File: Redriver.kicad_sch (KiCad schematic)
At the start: 126 parts, among them U1 DS320PR810NJXR, U2 DS320PR810NJXR

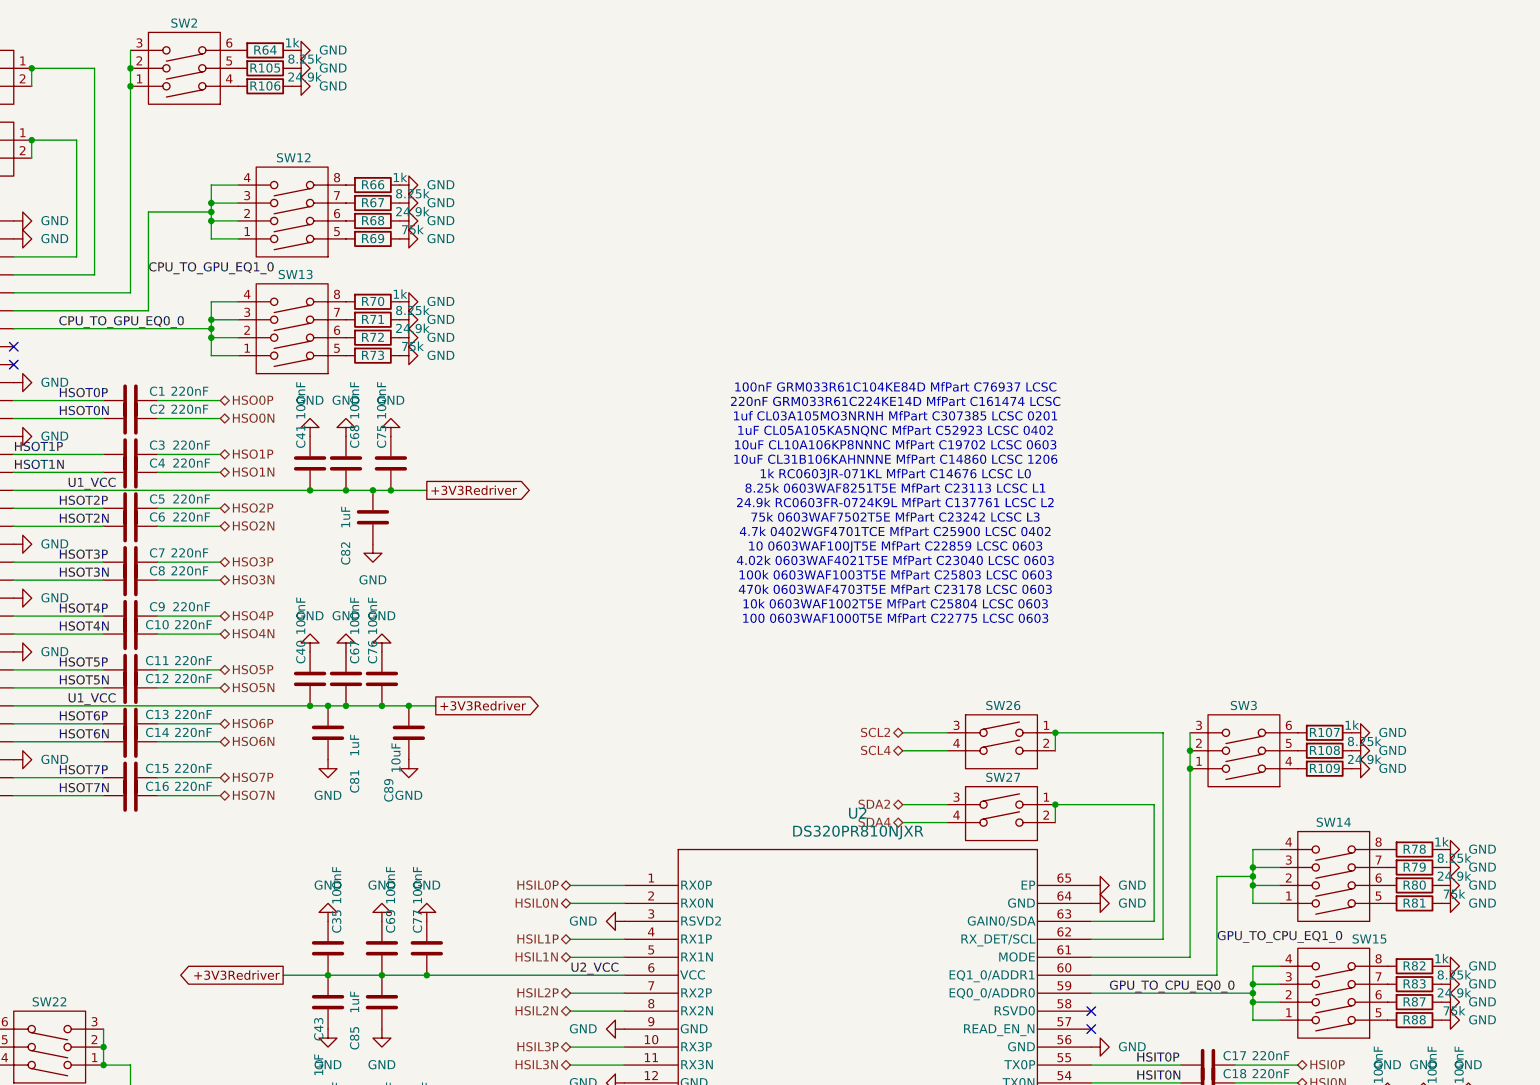
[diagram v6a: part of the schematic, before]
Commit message: removed uneeded mode
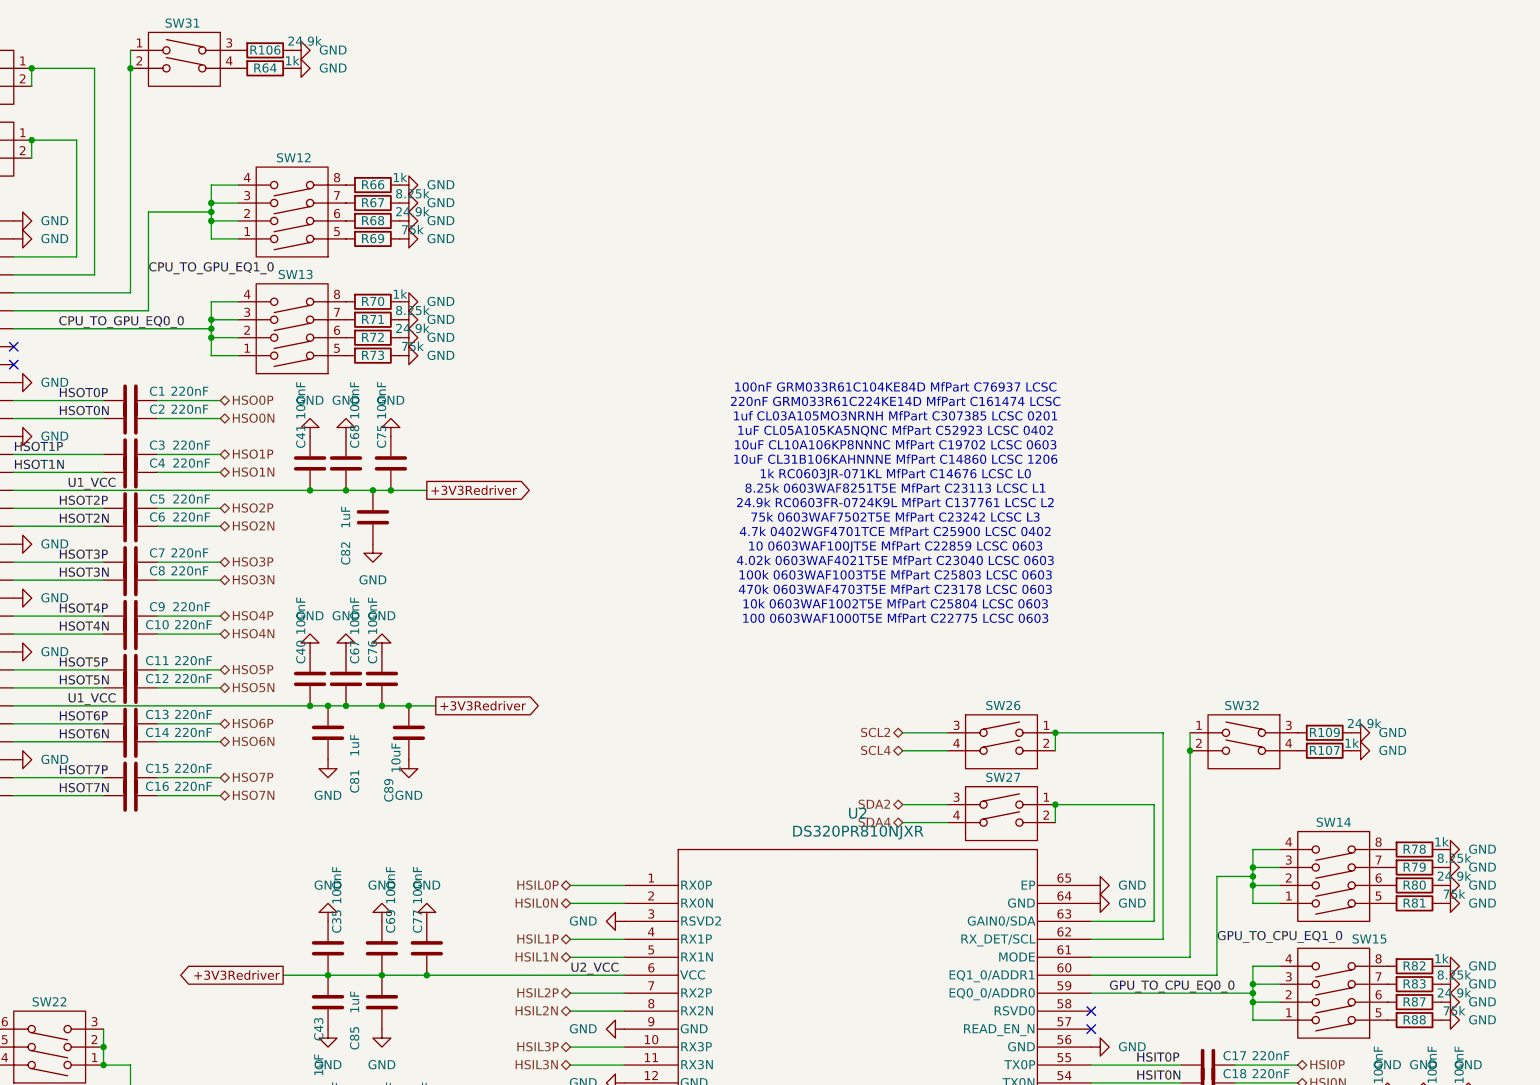
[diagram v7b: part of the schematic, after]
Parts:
- removed R105, R108: 8.25k, Resistor_SMD:R_0603_1608Metric, symbol Device:R
- removed SW2, SW3: ~, DSWB03LHGET:SW-TH_DSWB03LHGET, symbol DSWB03LHGET:DSWB03LHGET
- added SW31, SW32: ~, DSWB02LHGET:SW-TH_DSWB02LHGET, symbol DSWB02LHGET:DSWB02LHGET
- R106, R109: Part_Number 0603WAF8251T5E -> RC0603FR-0724K9L
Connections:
- net at R106.2: now also SW31.3
- net at U1.61 (MODE): now also SW31.1, SW31.2
- net at R64.2: now also SW31.4
- net at R107.2: now also SW32.4
- net at U2.61 (MODE): now also SW32.1, SW32.2
- net at R109.2: now also SW32.3
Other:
- moved on the sheet: R106, R107, R109, R64

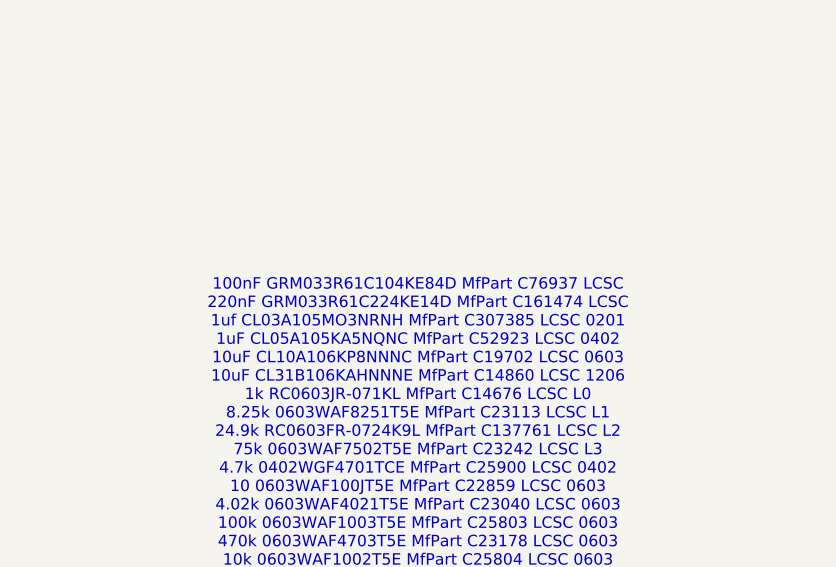
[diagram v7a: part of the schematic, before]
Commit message: added  better components
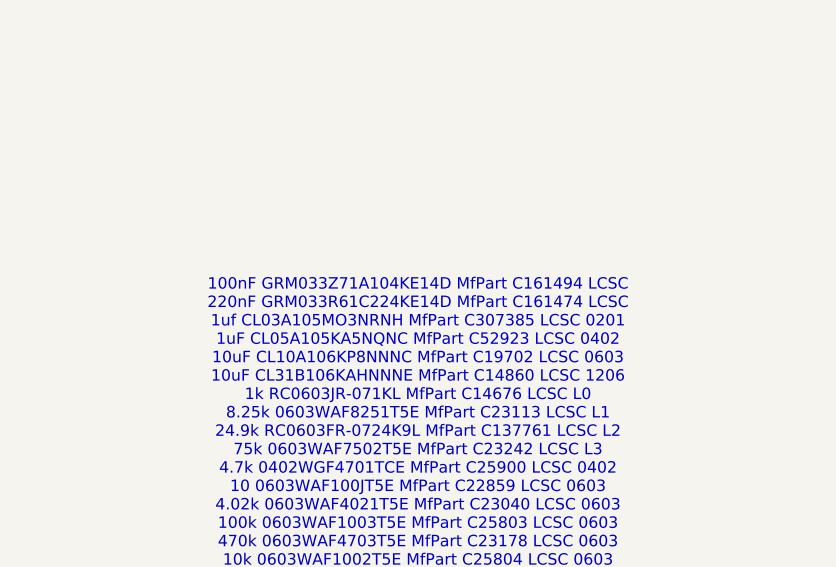
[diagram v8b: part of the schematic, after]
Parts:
- C33, C34, C35, C36, C38, C39, C40, C41, C65, C66, C67, C68, C69, C70, C71, C72, C73, C74, C75, C76, C77, C78, C79, C80: LCSC C76937 -> C161494; Part_Number GRM033R61C104KE84D -> GRM033Z71A104KE14D
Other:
- note added: "100nF GRM033Z71A104KE14D MfPart C161494 LCSC 220nF GRM033R61C224KE14D MfPart C161474 LCSC 1uf CL03A105MO3NRNH MfPart C307385 LCSC 0201 1uF CL05A105KA5NQNC MfPart C52923 LCSC 0402 10uF CL10A106KP8NNNC MfPart C19702 LCSC 0603 10uF CL31B106KAHNNNE MfPart C14860 LCSC 1206 1k RC0603JR-071KL MfPart C14676 LCSC L0 8.25k 0603WAF8251T5E MfPart C23113 LCSC L1 24.9k RC0603FR-0724K9L MfPart C137761 LCSC L2 7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"
- note removed: "100nF GRM033R61C104KE84D MfPart C76937 LCSC 220nF GRM033R61C224KE14D MfPart C161474 LCSC 1uf CL03A105MO3NRNH MfPart C307385 LCSC 0201 1uF CL05A105KA5NQNC MfPart C52923 LCSC 0402 10uF CL10A106KP8NNNC MfPart C19702 LCSC 0603 10uF CL31B106KAHNNNE MfPart C14860 LCSC 1206 1k RC0603JR-071KL MfPart C14676 LCSC L0 8.25k 0603WAF8251T5E MfPart C23113 LCSC L1 24.9k RC0603FR-0724K9L MfPart C137761 LCSC L2 75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"
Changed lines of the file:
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@@
 	(generator_version "9.0")
 	(paper "A4")
-	(text "100nF GRM033R61C104KE84D MfPart C76937 LCSC\n220nF GRM033R61C224KE14D MfPart C161474 LCSC\n1uf CL03A105MO3NRNH MfPart C307385 LCSC 0201\n1uF CL05A105KA5NQNC MfPart C52923 LCSC 0402\n10uF CL10A106KP8NNNC MfPart C19702 LCSC 0603\n10uF CL31B106KAHNNNE MfPart C14860 LCSC 1206\n1k RC0603JR-071KL MfPart C14676 LCSC L0\n8.25k 0603WAF8251T5E MfPart C23113 LCSC L1\n24.9k RC0603FR-0724K9L MfPart C137761 LCSC L2\n75k 0603WAF7502T5E MfPart C23242 LCSC L3\n4.7k 0402WGF4701TCE MfPart C25900 LCSC 0402\n10 0603WAF100JT5E MfPart C22859 LCSC 0603\n4.02k 0603WAF4021T5E MfPart C23040 LCSC 0603\n100k 0603WAF1003T5E MfPart C25803 LCSC 0603\n470k 0603WAF4703T5E MfPart C23178 LCSC 0603\n10k 0603WAF1002T5E MfPart C25804 LCSC 0603\n100 0603WAF1000T5E MfPart C22775 LCSC 0603"
+	(text "100nF GRM033Z71A104KE14D MfPart C161494 LCSC\n220nF GRM033R61C224KE14D MfPart C161474 LCSC\n1uf CL03A105MO3NRNH MfPart C307385 LCSC 0201\n1uF CL05A105KA5NQNC MfPart C52923 LCSC 0402\n10uF CL10A106KP8NNNC MfPart C19702 LCSC 0603\n10uF CL31B106KAHNNNE MfPart C14860 LCSC 1206\n1k RC0603JR-071KL MfPart C14676 LCSC L0\n8.25k 0603WAF8251T5E MfPart C23113 LCSC L1\n24.9k RC0603FR-0724K9L MfPart C137761 LCSC L2\n75k 0603WAF7502T5E MfPart C23242 LCSC L3\n4.7k 0402WGF4701TCE MfPart C25900 LCSC 0402\n10 0603WAF100JT5E MfPart C22859 LCSC 0603\n4.02k 0603WAF4021T5E MfPart C23040 LCSC 0603\n100k 0603WAF1003T5E MfPart C25803 LCSC 0603\n470k 0603WAF4703T5E MfPart C23178 LCSC 0603\n10k 0603WAF1002T5E MfPart C25804 LCSC 0603\n100 0603WAF1000T5E MfPart C22775 LCSC 0603"
 		(exclude_from_sim no)
 		(at 250.444 24.892 0)
@@
 			)
 		)
-		(property "Part_Number" "GRM033R61C104KE84D"
+		(property "Part_Number" "GRM033Z71A104KE14D"
 			(at 170.18 118.11 0)
 			(effects
@@
 			)
 		)
-		(property "LCSC" "C76937"
+		(property "LCSC" "C161494"
 			(at 170.18 118.11 0)
 			(effects
@@
 			)
 		)
-		(property "Part_Number" "GRM033R61C104KE84D"
+		(property "Part_Number" "GRM033Z71A104KE14D"
 			(at 330.2 143.51 0)
 			(effects
@@
 			)
 		)
-		(property "LCSC" "C76937"
+		(property "LCSC" "C161494"
 			(at 330.2 143.51 0)
 			(effects
@@
 			)
 		)
-		(property "Part_Number" "GRM033R61C104KE84D"
+		(property "Part_Number" "GRM033Z71A104KE14D"
 			(at 167.64 49.53 0)
 			(effects
@@
 			)
 		)
-		(property "LCSC" "C76937"
+		(property "LCSC" "C161494"
 			(at 167.64 49.53 0)
 			(effects
@@
 			)
 		)
-		(property "Part_Number" "GRM033R61C104KE84D"
+		(property "Part_Number" "GRM033Z71A104KE14D"
 			(at 320.04 143.51 0)
 			(effects
@@
 			)
 		)
-		(property "LCSC" "C76937"
+		(property "LCSC" "C161494"
 			(at 320.04 143.51 0)
 			(effects
@@
 			)
 		)
-		(property "Part_Number" "GRM033R61C104KE84D"
+		(property "Part_Number" "GRM033Z71A104KE14D"
 			(at 167.64 19.05 0)
 			(effects
@@
 			)
 		)
-		(property "LCSC" "C76937"
+		(property "LCSC" "C161494"
 			(at 167.64 19.05 0)
 			(effects
@@
 			)
 		)
-		(property "Part_Number" "GRM033R61C104KE84D"
+		(property "Part_Number" "GRM033Z71A104KE14D"
 			(at 26.67 -6.35 0)
 			(effects
@@
 			)
 		)
-		(property "LCSC" "C76937"
+		(property "LCSC" "C161494"
 			(at 26.67 -6.35 0)
 			(effects
@@
 			)
 		)
-		(property "Part_Number" "GRM033R61C104KE84D"
+		(property "Part_Number" "GRM033Z71A104KE14D"
 			(at 179.07 19.05 0)
 			(effects
@@
 			)
 		)
-		(property "LCSC" "C76937"
+		(property "LCSC" "C161494"
 			(at 179.07 19.05 0)
 			(effects
@@
 			)
 		)
-		(property "Part_Number" "GRM033R61C104KE84D"
+		(property "Part_Number" "GRM033Z71A104KE14D"
 			(at 185.42 118.11 0)
 			(effects
@@
 			)
 		)
-		(property "LCSC" "C76937"
+		(property "LCSC" "C161494"
 			(at 185.42 118.11 0)
 			(effects
@@
 			)
 		)
-		(property "Part_Number" "GRM033R61C104KE84D"
+		(property "Part_Number" "GRM033Z71A104KE14D"
 			(at 38.1 24.13 0)
 			(effects
@@
 			)
 		)
-		(property "LCSC" "C76937"
+		(property "LCSC" "C161494"
 			(at 38.1 24.13 0)
 			(effects
@@
 			)
 		)
-		(property "Part_Number" "GRM033R61C104KE84D"
+		(property "Part_Number" "GRM033Z71A104KE14D"
 			(at 177.8 49.53 0)
 			(effects
@@
 			)
 		)
-		(property "LCSC" "C76937"
+		(property "LCSC" "C161494"
 			(at 177.8 49.53 0)
 			(effects
@@
 			)
 		)
-		(property "Part_Number" "GRM033R61C104KE84D"
+		(property "Part_Number" "GRM033Z71A104KE14D"
 			(at 172.72 49.53 0)
 			(effects
@@
 			)
 		)
-		(property "LCSC" "C76937"
+		(property "LCSC" "C161494"
 			(at 172.72 49.53 0)
 			(effects
@@
 			)
 		)
-		(property "Part_Number" "GRM033R61C104KE84D"
+		(property "Part_Number" "GRM033Z71A104KE14D"
 			(at 39.37 -6.35 0)
 			(effects
@@
 			)
 		)
-		(property "LCSC" "C76937"
+		(property "LCSC" "C161494"
 			(at 39.37 -6.35 0)
 			(effects
@@
 			)
 		)
-		(property "Part_Number" "GRM033R61C104KE84D"
+		(property "Part_Number" "GRM033Z71A104KE14D"
 			(at 172.72 19.05 0)
 			(effects
@@
 			)
 		)
-		(property "LCSC" "C76937"
+		(property "LCSC" "C161494"
 			(at 172.72 19.05 0)
 			(effects
@@
 			)
 		)
-		(property "Part_Number" "GRM033R61C104KE84D"
+		(property "Part_Number" "GRM033Z71A104KE14D"
 			(at 184.15 87.63 0)
 			(effects
@@
 			)
 		)
-		(property "LCSC" "C76937"
+		(property "LCSC" "C161494"
 			(at 184.15 87.63 0)
 			(effects
@@
 			)
 		)
-		(property "Part_Number" "GRM033R61C104KE84D"
+		(property "Part_Number" "GRM033Z71A104KE14D"
 			(at 34.29 -6.35 0)
 			(effects
@@
 			)
 		)
-		(property "LCSC" "C76937"
+		(property "LCSC" "C161494"
 			(at 34.29 -6.35 0)
 			(effects
@@
 			)
 		)
-		(property "Part_Number" "GRM033R61C104KE84D"
+		(property "Part_Number" "GRM033Z71A104KE14D"
 			(at 170.18 87.63 0)
 			(effects
@@
 			)
 		)
-		(property "LCSC" "C76937"
+		(property "LCSC" "C161494"
 			(at 170.18 87.63 0)
 			(effects
@@
 			)
 		)
-		(property "Part_Number" "GRM033R61C104KE84D"
+		(property "Part_Number" "GRM033Z71A104KE14D"
 			(at 325.12 143.51 0)
 			(effects
@@
 			)
 		)
-		(property "LCSC" "C76937"
+		(property "LCSC" "C161494"
 			(at 325.12 143.51 0)
 			(effects
@@
 			)
 		)
-		(property "Part_Number" "GRM033R61C104KE84D"
+		(property "Part_Number" "GRM033Z71A104KE14D"
 			(at 26.67 24.13 0)
 			(effects
@@
 			)
 		)
-		(property "LCSC" "C76937"
+		(property "LCSC" "C161494"
 			(at 26.67 24.13 0)
 			(effects
@@
 			)
 		)
-		(property "Part_Number" "GRM033R61C104KE84D"
+		(property "Part_Number" "GRM033Z71A104KE14D"
 			(at 331.47 113.03 0)
 			(effects
@@
 			)
 		)
-		(property "LCSC" "C76937"
+		(property "LCSC" "C161494"
 			(at 331.47 113.03 0)
 			(effects
@@
 			)
 		)
-		(property "Part_Number" "GRM033R61C104KE84D"
+		(property "Part_Number" "GRM033Z71A104KE14D"
 			(at 177.8 118.11 0)
 			(effects
@@
 			)
 		)
-		(property "LCSC" "C76937"
+		(property "LCSC" "C161494"
 			(at 177.8 118.11 0)
 			(effects
@@
 			)
 		)
-		(property "Part_Number" "GRM033R61C104KE84D"
+		(property "Part_Number" "GRM033Z71A104KE14D"
 			(at 320.04 113.03 0)
 			(effects
@@
 			)
 		)
-		(property "LCSC" "C76937"
+		(property "LCSC" "C161494"
 			(at 320.04 113.03 0)
 			(effects
@@
 			)
 		)
-		(property "Part_Number" "GRM033R61C104KE84D"
+		(property "Part_Number" "GRM033Z71A104KE14D"
 			(at 325.12 113.03 0)
 			(effects
@@
 			)
 		)
-		(property "LCSC" "C76937"
+		(property "LCSC" "C161494"
 			(at 325.12 113.03 0)
 			(effects
@@
 			)
 		)
-		(property "Part_Number" "GRM033R61C104KE84D"
+		(property "Part_Number" "GRM033Z71A104KE14D"
 			(at 177.8 87.63 0)
 			(effects
@@
 			)
 		)
-		(property "LCSC" "C76937"
+		(property "LCSC" "C161494"
 			(at 177.8 87.63 0)
 			(effects
@@
 			)
 		)
-		(property "Part_Number" "GRM033R61C104KE84D"
+		(property "Part_Number" "GRM033Z71A104KE14D"
 			(at 33.02 24.13 0)
 			(effects
@@
 			)
 		)
-		(property "LCSC" "C76937"
+		(property "LCSC" "C161494"
 			(at 33.02 24.13 0)
 			(effects
